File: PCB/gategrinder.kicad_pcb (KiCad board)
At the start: 2 copper layers, 96 x 196 mm, 71 parts, among them J1 EURO_PWR_2x5, J10 AudioJack3_SwitchTR, J3 Conn_01x14, J6 AudioJack3_SwitchTR, J7 AudioJack3_SwitchTR, J8 AudioJack3_SwitchTR, J9 AudioJack3_SwitchTR, Q1 BC547, Q2 BC547, Q3 BC547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

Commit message: Rotate
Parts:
- moved D1 145.1 mm to (50.7, 85.8), turned to 90 degrees
- moved C5 142.5 mm to (51.0, 92.5), turned to 270 degrees
- moved J1 140.3 mm to (61.0, 68.8), turned to 90 degrees
- moved C7 139.7 mm to (52.0, 129.2), turned to 90 degrees
- moved D2 136.2 mm to (61.0, 75.6), turned to 270 degrees
- moved D3 134.1 mm to (55.0, 106.0), turned to 270 degrees
- moved U3 134.1 mm to (55.0, 121.0), turned to 270 degrees
- moved C6 128.1 mm to (61.0, 94.4), turned to 90 degrees
- moved R7 127.1 mm to (60.0, 106.0), turned to 270 degrees
- moved R8 119.5 mm to (65.0, 113.6), turned to 90 degrees
- moved C8 118.9 mm to (65.7, 120.5), turned to 270 degrees
- moved C10 118.8 mm to (67.0, 129.0), turned to 90 degrees
- moved J8 117.0 mm to (208.5, 55.5), turned to 90 degrees
- moved REF** 114.7 mm to (71.0, 93.0), turned to 270 degrees
- moved U4 113.0 mm to (70.0, 121.0), turned to 270 degrees
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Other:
- board size 96 x 196 mm -> 196 x 96 mm

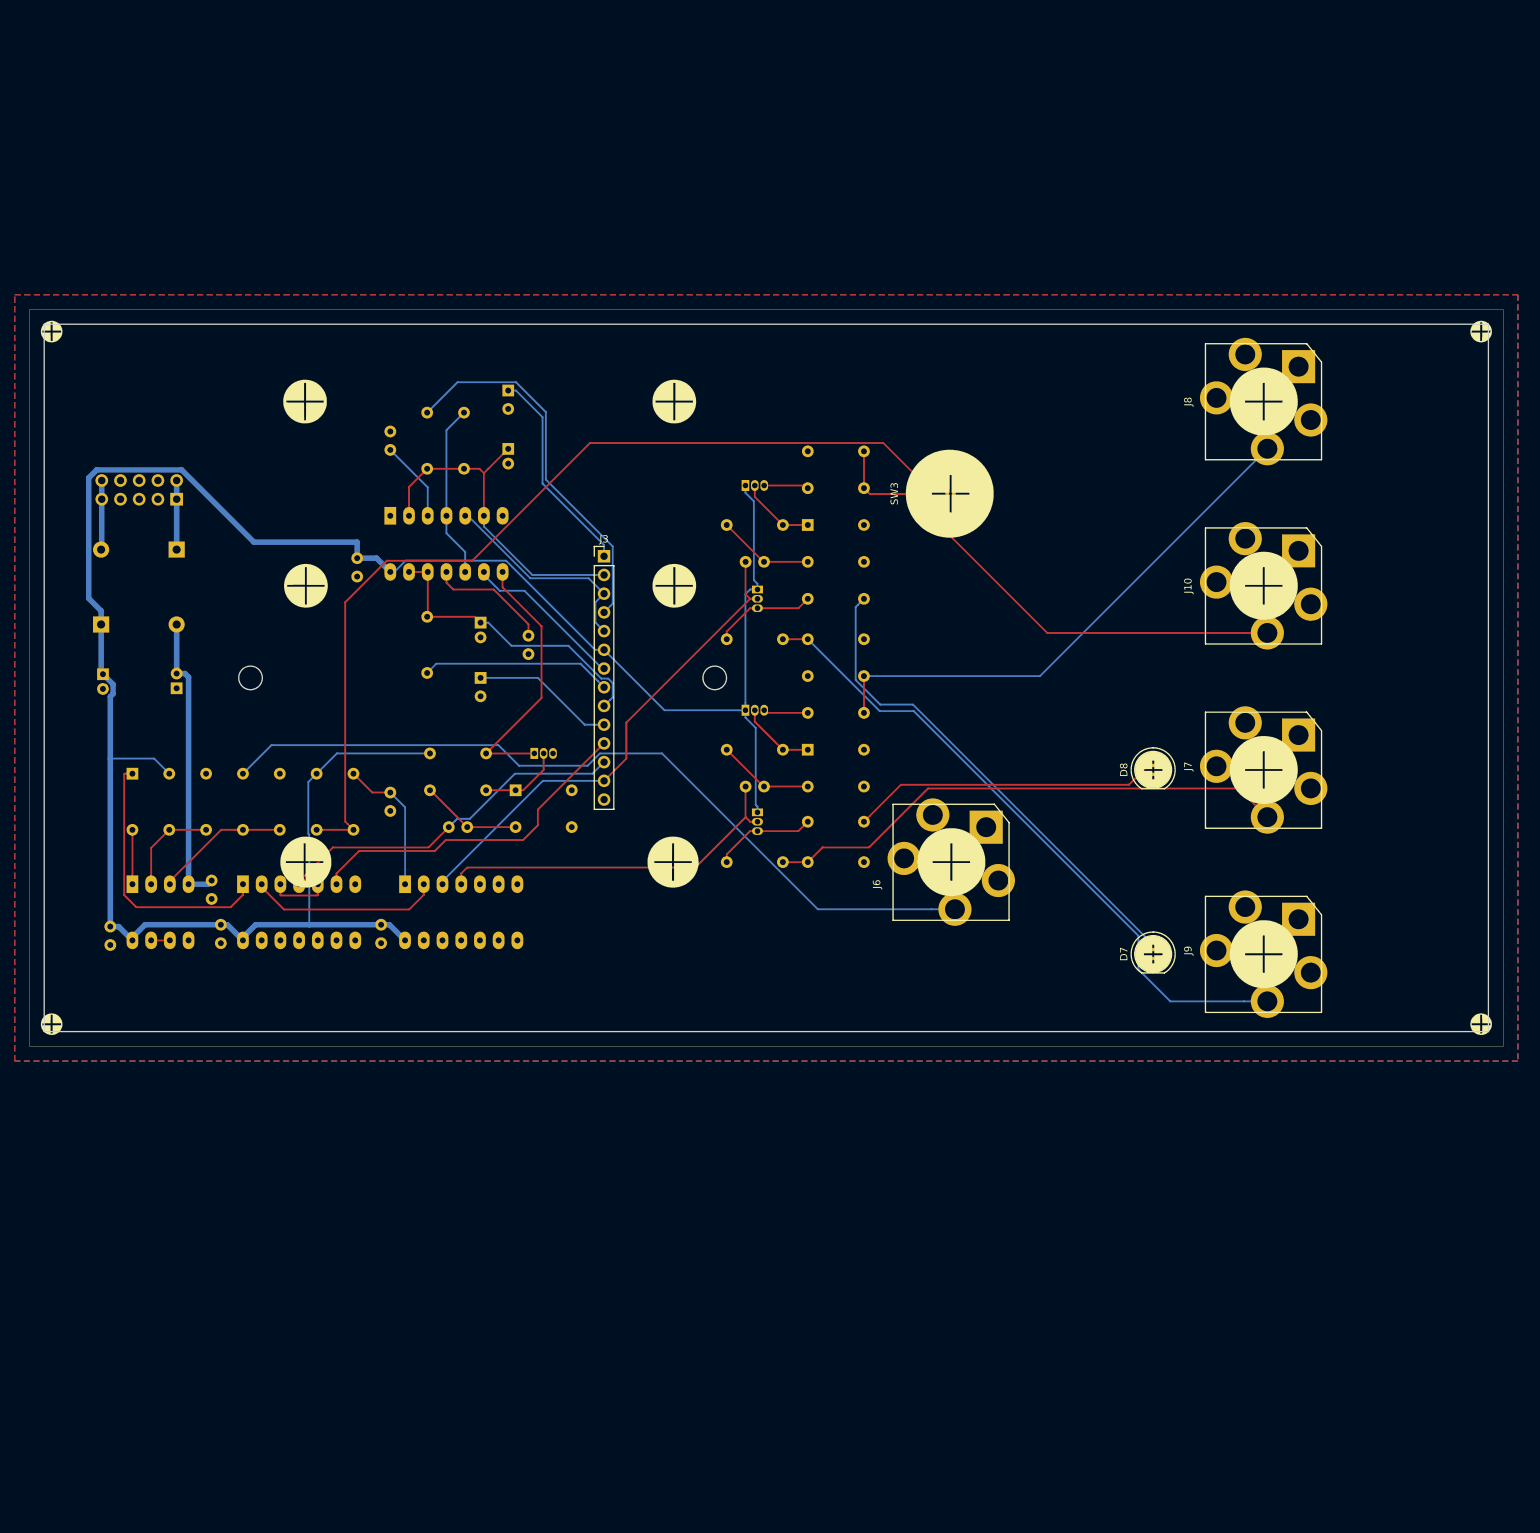
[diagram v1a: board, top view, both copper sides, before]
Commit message: Libraries cleanup and silkscreen work
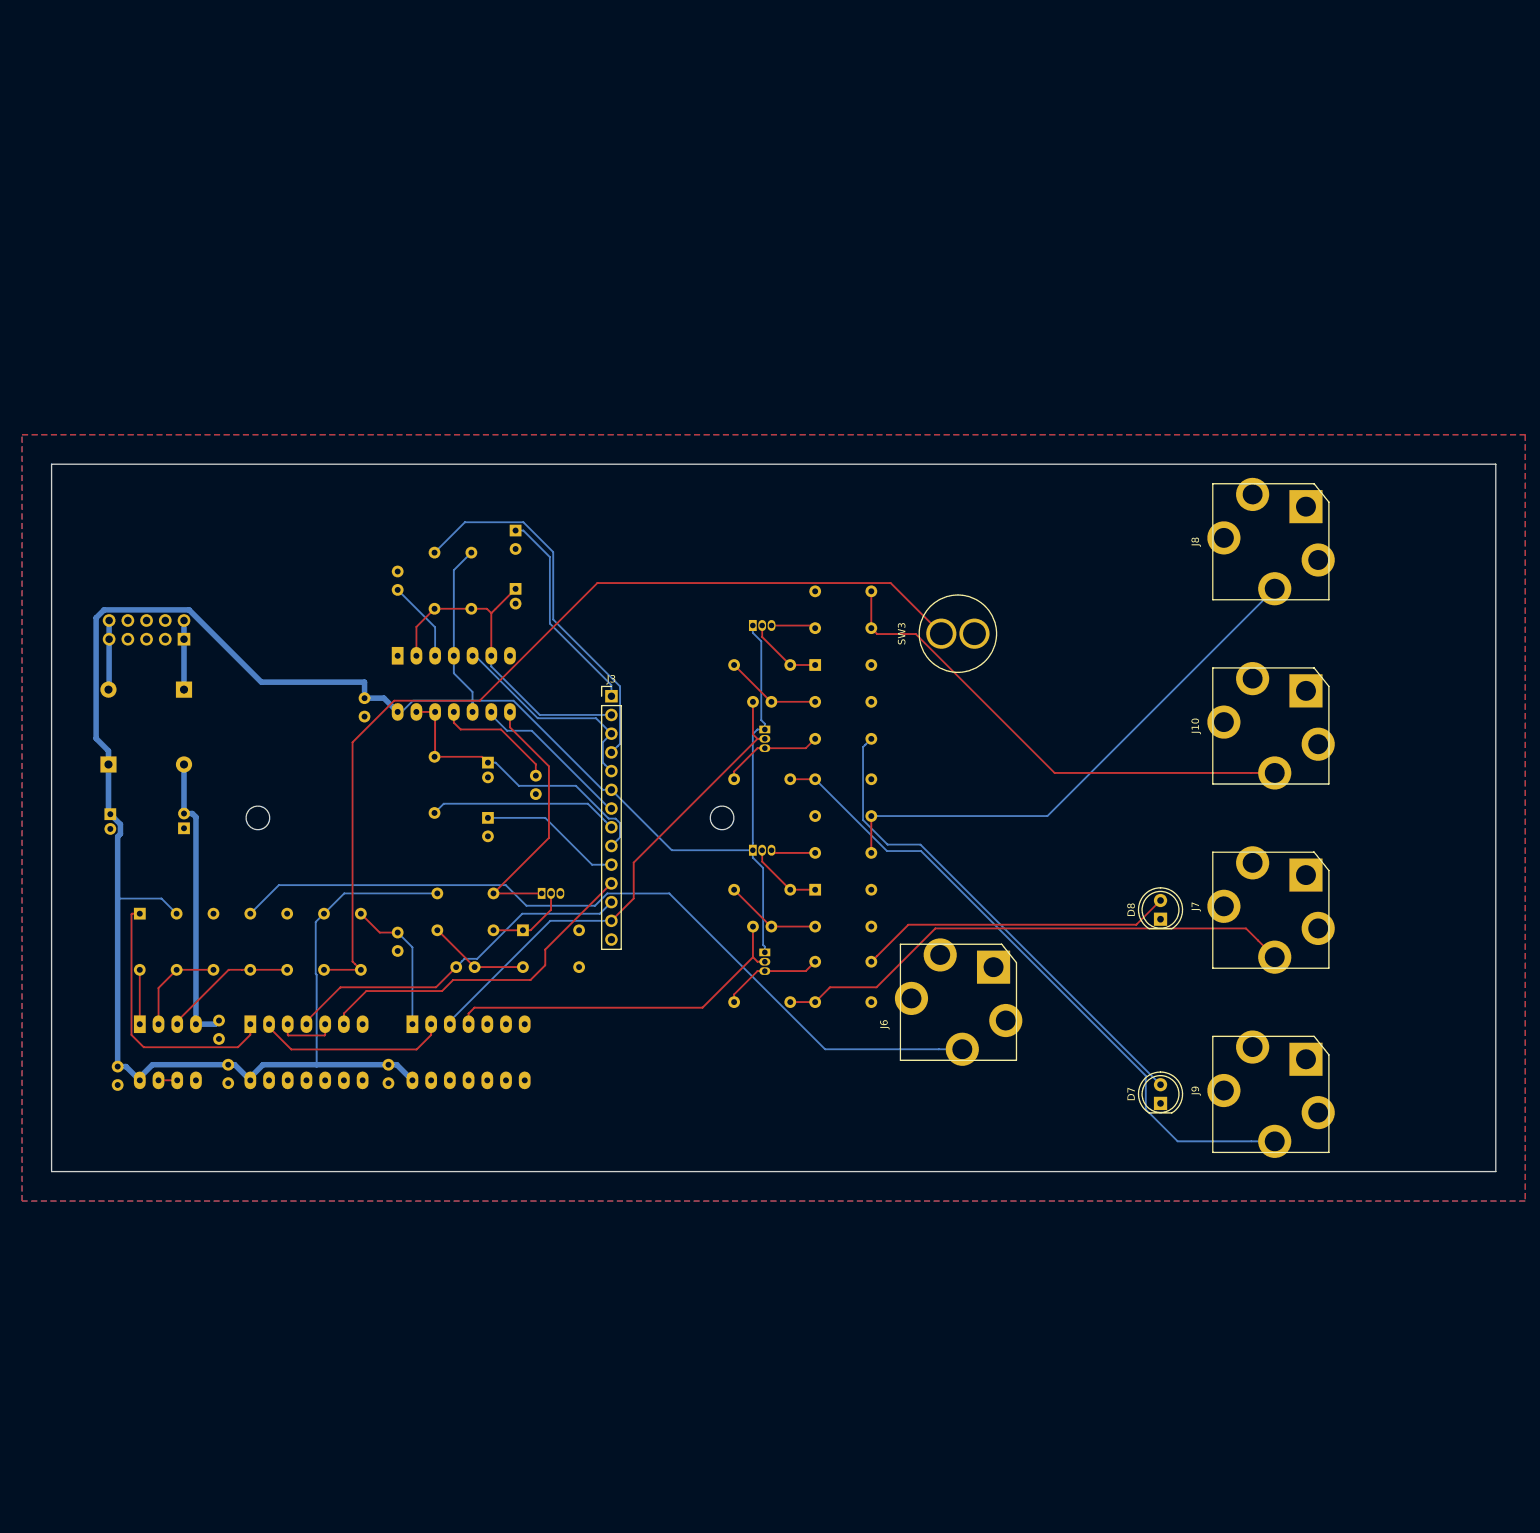
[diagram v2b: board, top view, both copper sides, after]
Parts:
- removed the G*** at (141.0, 93.0)
- removed the REF** at (134.0, 93.0)
- removed the REF** at (71.0, 93.0)
- added G***: LOGO, Gate Grinder:analogoutput2, B.Cu at (229.0, 112.0)
- added G***: LOGO, Gate Grinder:Gate_Grinder_panel_holes, F.Cu at (142.0, 112.0)
- added REF**: MountingHole_3.2mm_M3, MountingHole:MountingHole_3.2mm_M3, B.Cu at (135.0, 112.0)
- added REF**: MountingHole_3.2mm_M3, MountingHole:MountingHole_3.2mm_M3, B.Cu at (72.0, 112.0)
- moved R15 19.0 mm to (155.2, 131.5)
- moved C1 19.0 mm to (91.0, 81.1)
- moved C10 19.0 mm to (68.0, 148.0)
- moved C11 19.0 mm to (89.7, 148.0)
- moved C12 19.0 mm to (109.7, 106.3)
- moved C13 19.0 mm to (86.5, 95.8)
- moved C14 19.0 mm to (103.2, 104.5)
- moved C15 19.0 mm to (139.2, 126.8)
- moved C16 19.0 mm to (139.2, 96.2)
- moved C17 19.0 mm to (103.2, 112.0)
- moved C2 19.0 mm to (107.0, 80.9)
- moved C3 19.0 mm to (91.0, 127.6)
- moved C4 19.0 mm to (107.0, 73.0)
- moved C5 19.0 mm to (52.0, 111.5)
- moved C6 19.0 mm to (62.0, 113.4)
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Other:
- board text added: "Gate Grinder"
- board text added: "Rich Holmes 5/2020"

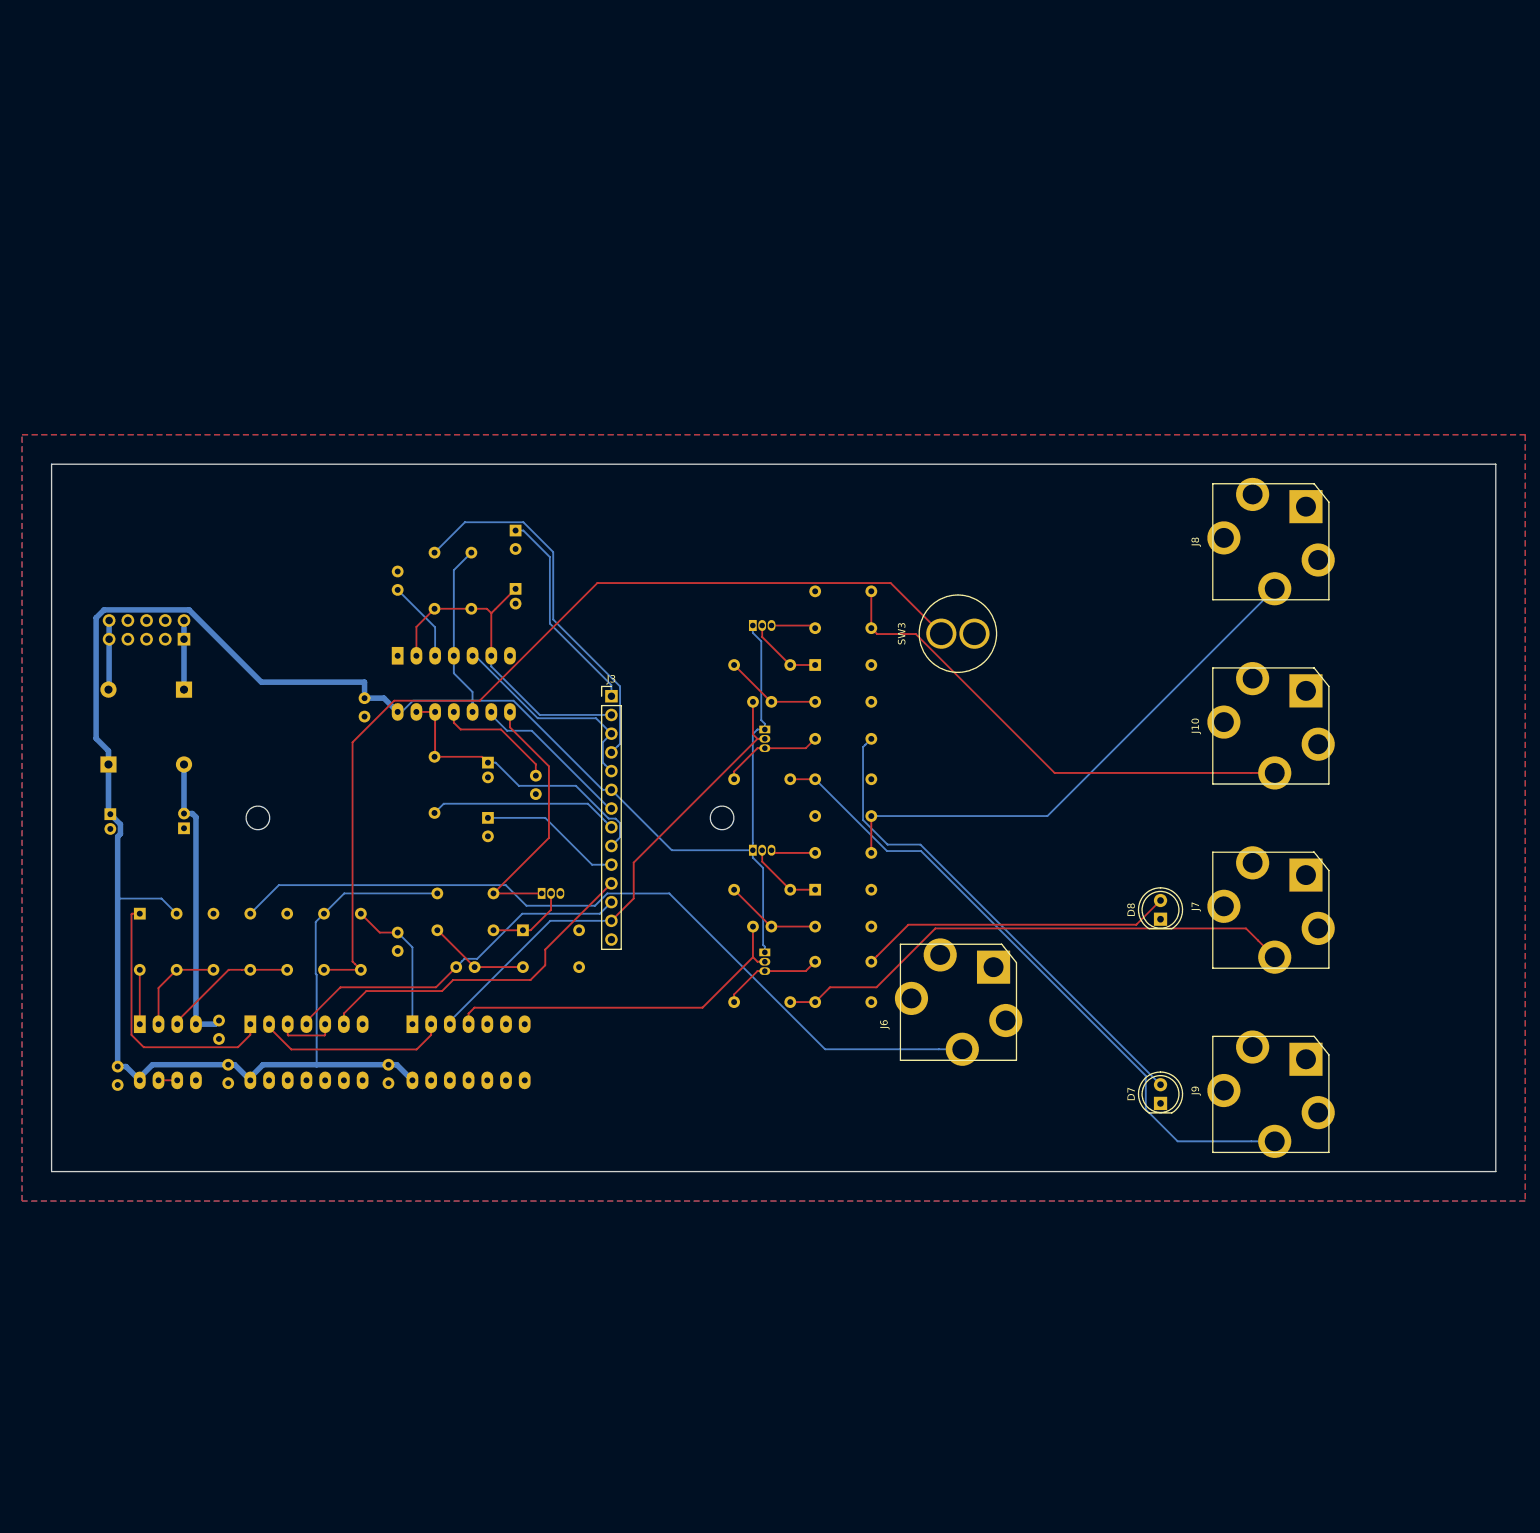
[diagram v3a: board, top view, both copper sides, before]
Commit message: Shorten main board; widen transistor footprints
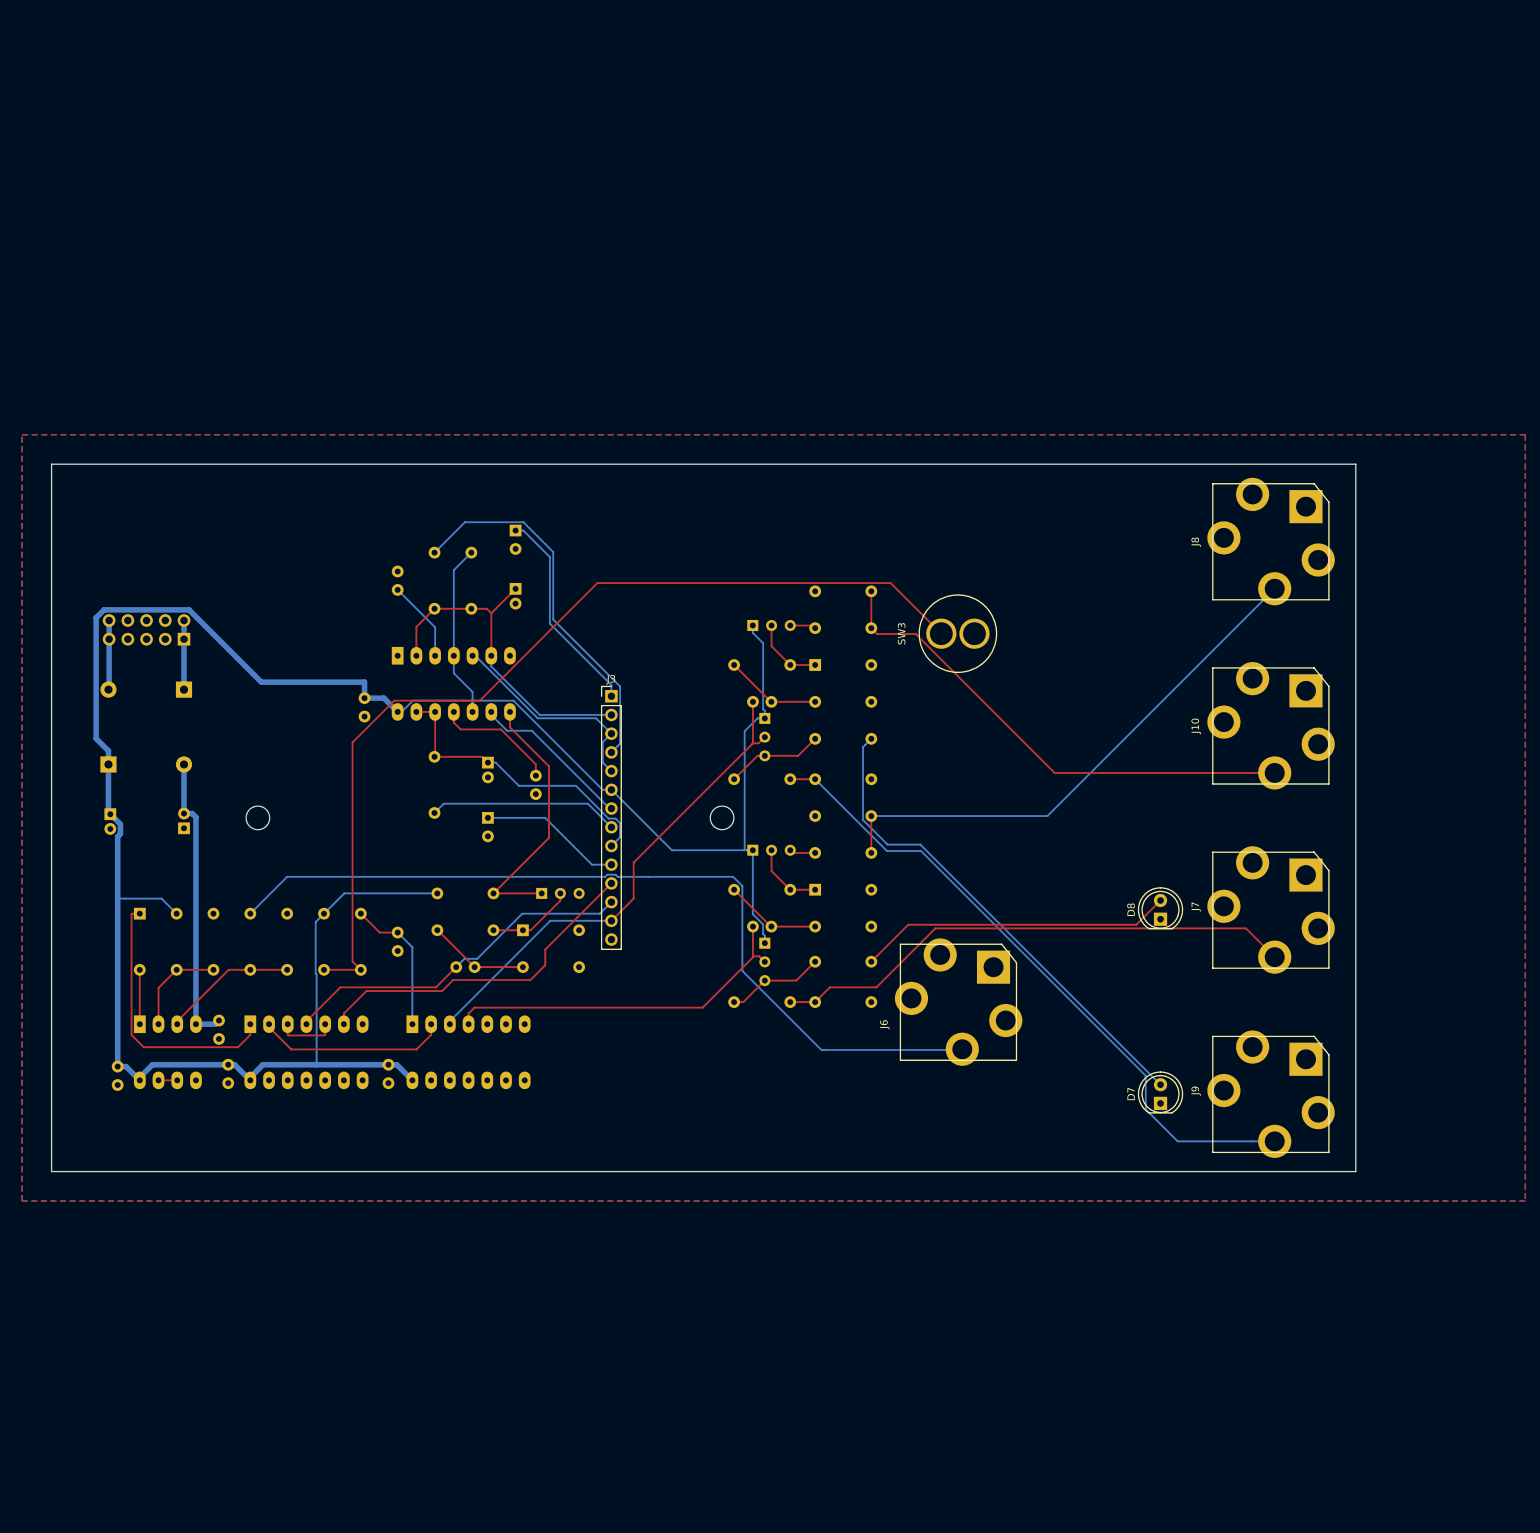
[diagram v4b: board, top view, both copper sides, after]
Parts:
- Q1, Q2, Q3, Q4, Q5: footprint Package_TO_SOT_THT:TO-92_Inline -> Package_TO_SOT_THT:TO-92_Inline_Wide
- moved G*** 46.0 mm to (183.0, 112.0)
- moved Q3 1.50 mm to (140.8, 98.5)
- moved Q2 1.25 mm to (140.8, 129.0)
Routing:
- net /GATE_IN: track 108.8 -> 115.9 mm
- net Net-(Q4-Pad3): track 6.07 -> 3.53 mm
- net Net-(Q5-Pad3): track 6.07 -> 3.53 mm
- net Net-(Q3-Pad3): track 13.9 -> 13.3 mm
- net Net-(Q2-Pad3): track 13.9 -> 13.3 mm
- net Net-(D6-Pad1): track 10.3 -> 9.79 mm
- net Net-(D4-Pad1): track 11.2 -> 11.7 mm
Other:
- board size 196 x 96 mm -> 177 x 96 mm

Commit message: BOMs and build notes
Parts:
- removed the G*** at (142.0, 112.0)
